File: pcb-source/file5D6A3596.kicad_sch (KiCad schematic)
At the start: 23 parts, among them J2 Program_enable, J4 UPDI, J6 Conn_02x03_Odd_Even, U2 MAX3232, U5 MCP795xx, Y1 32KHz

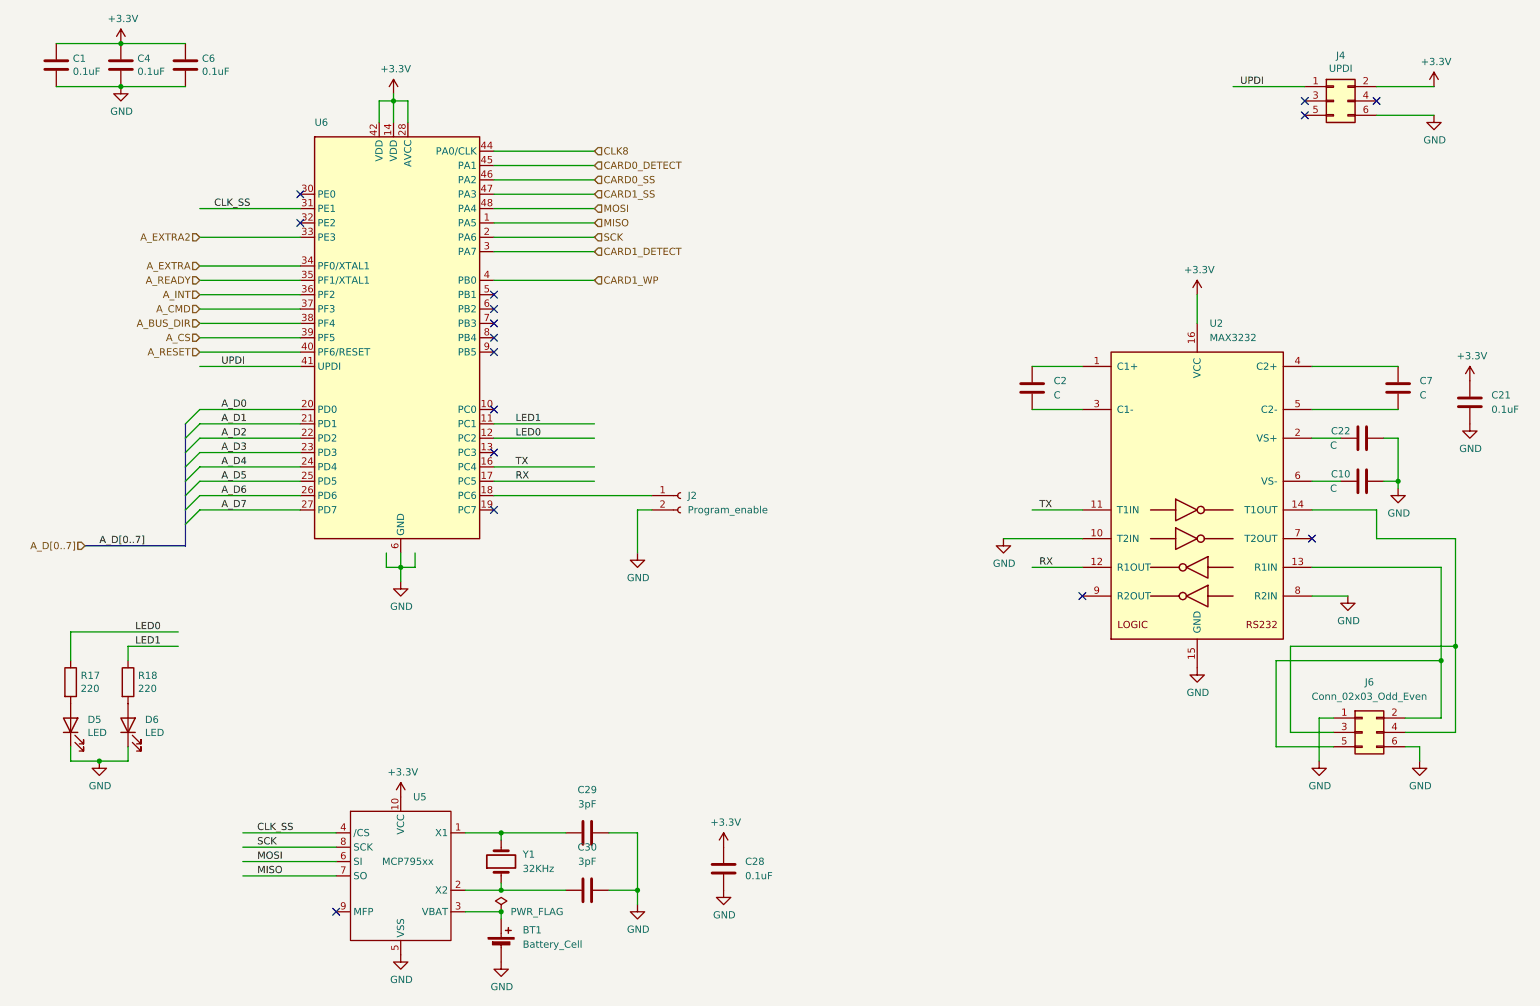
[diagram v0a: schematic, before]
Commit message: STM32C01 version, now in a working state (#6)
Code for V2 board, proven and now working.
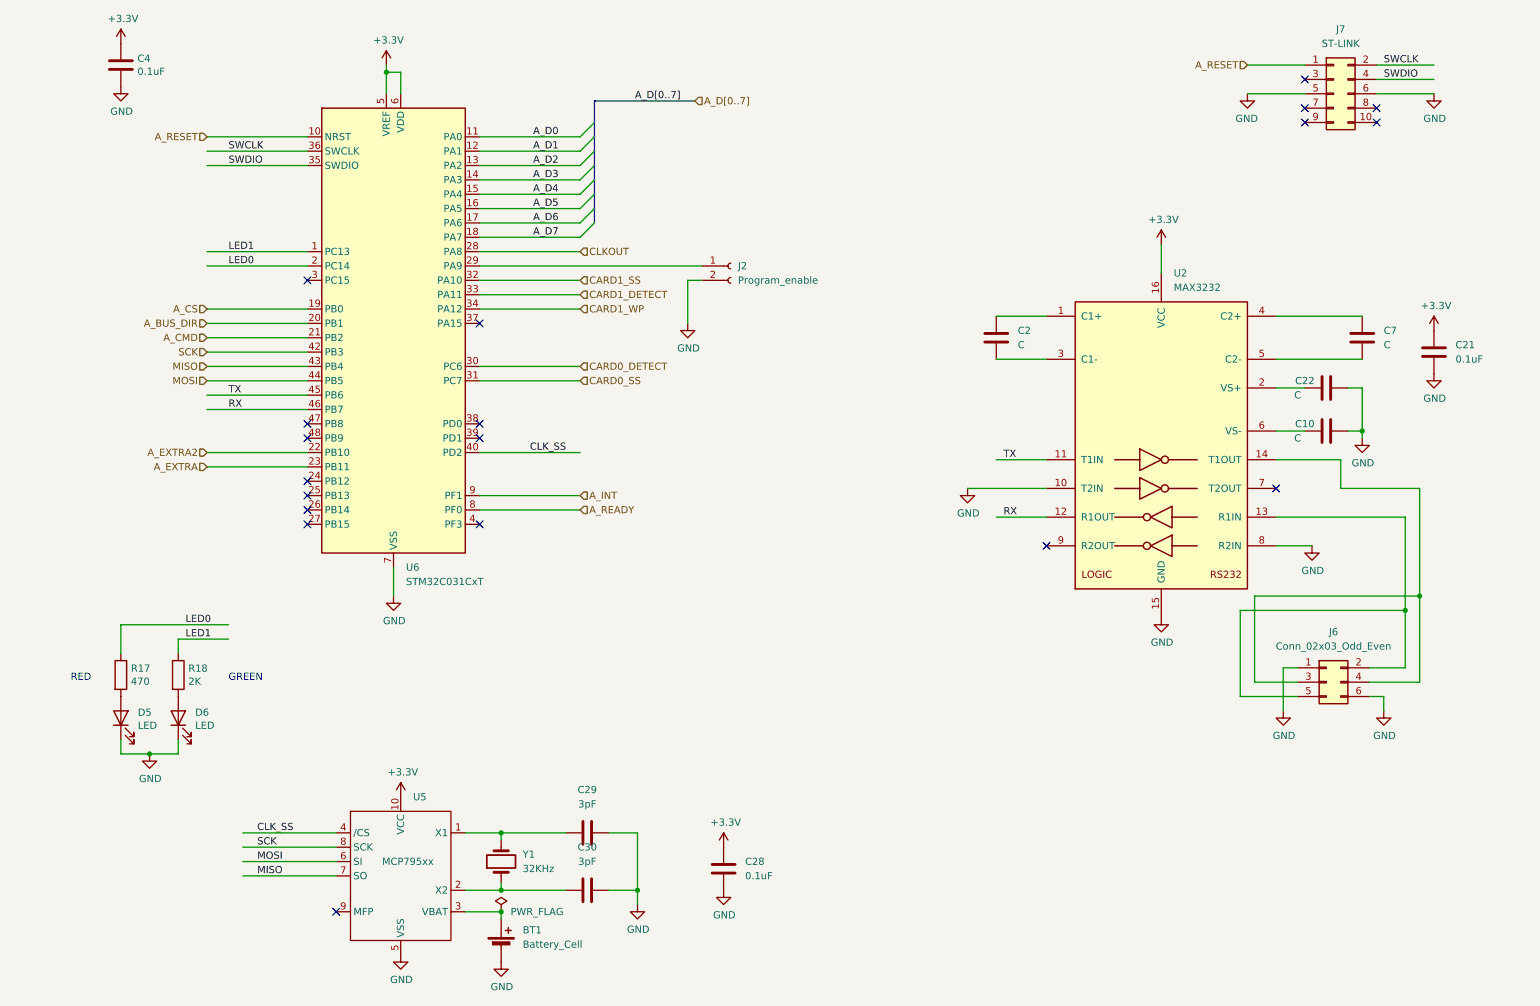
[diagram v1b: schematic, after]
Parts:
- removed C1, C6: 0.1uF, Capacitor_SMD:C_0603_1608Metric, symbol Device:C
- removed J4: UPDI, Connector_PinHeader_2.54mm:PinHeader_2x03_P2.54mm_Vertical, symbol Connector_Generic:Conn_02x03_Odd_Even
- removed U6: ~, Package_QFP:LQFP-48_7x7mm_P0.5mm, symbol Simon:AVR128DA-48
- added J7: ST-LINK, Connector_PinHeader_2.54mm:PinHeader_2x05_P2.54mm_Vertical, symbol Connector_Generic:Conn_02x05_Odd_Even
- added U6: STM32C031CxT, Package_QFP:LQFP-48_7x7mm_P0.5mm, symbol Simon:STM32C031CxT
- R17: value 220 -> 470
- R18: value 220 -> 2K
- Y1: footprint Crystal:Crystal_C38-LF_D3.0mm_L8.0mm_Vertical -> simon:Crystal_SMD_ECX_31B-2Pin_3.2x1.5mm
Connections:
- net +3V3: now also U6.5 (VREF), U6.6 (VDD)
- net A_BUS_DIR: now also U6.20 (PB1)
- net A_CMD: now also U6.21 (PB2)
- net A_CS: now also U6.19 (PB0)
- net A_D0: now also U6.11 (PA0)
- net A_D1: now also U6.12 (PA1)
- net A_D2: now also U6.13 (PA2)
- net A_D3: now also U6.14 (PA3)
- net A_D4: now also U6.15 (PA4)
- net A_D5: now also U6.16 (PA5)
- net A_D6: now also U6.17 (PA6)
- net A_D7: now also U6.18 (PA7)
- net A_EXTRA: now also U6.23 (PB11)
- net A_EXTRA2: now also U6.22 (PB10)
- net A_INT: now also U6.9 (PF1)
- net A_READY: now also U6.8 (PF0)
- net A_RESET: now also J7.1 (Pin_1), U6.10 (NRST)
- net CARD0_DETECT: now also U6.30 (PC6)
- net CARD0_SS: now also U6.31 (PC7)
- net CARD1_DETECT: now also U6.33 (PA11)
- net CARD1_SS: now also U6.32 (PA10)
- net CARD1_WP: now also U6.34 (PA12)
- net CLK_SS: now also U6.40 (PD2)
- net GND: now also J7.5 (Pin_5), J7.6 (Pin_6), U6.7 (VSS)
- net LED0: now also U6.2 (PC14)
- net LED1: now also U6.1 (PC13)
- net MISO: now also U6.43 (PB4)
- net MOSI: now also U6.44 (PB5)
- net RX: now also U6.46 (PB7)
- net SCK: now also U6.42 (PB3)
- net TX: now also U6.45 (PB6)
- net at J2.1 (Pin_1): now also U6.29 (PA9)
- new net CLKOUT: U6.28 (PA8)
- new net SWCLK: J7.2 (Pin_2), U6.36 (SWCLK)
- new net SWDIO: J7.4 (Pin_4), U6.35 (SWDIO)
- no-connect marks 16 -> 19
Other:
- note added: "GREEN"
- note added: "RED"
- moved on the sheet: C10, C2, C21, C22, C7, D5, D6, J2, J6, R17, R18, U2
